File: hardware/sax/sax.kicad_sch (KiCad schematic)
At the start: 36 parts, among them J101 Cortex, J102 DX07S016JA3, SW101 SKSG, SW102 SKSG, U101 TPS78433QWDRBRQ1, U102 ATSAMD51J, Y101 32k768

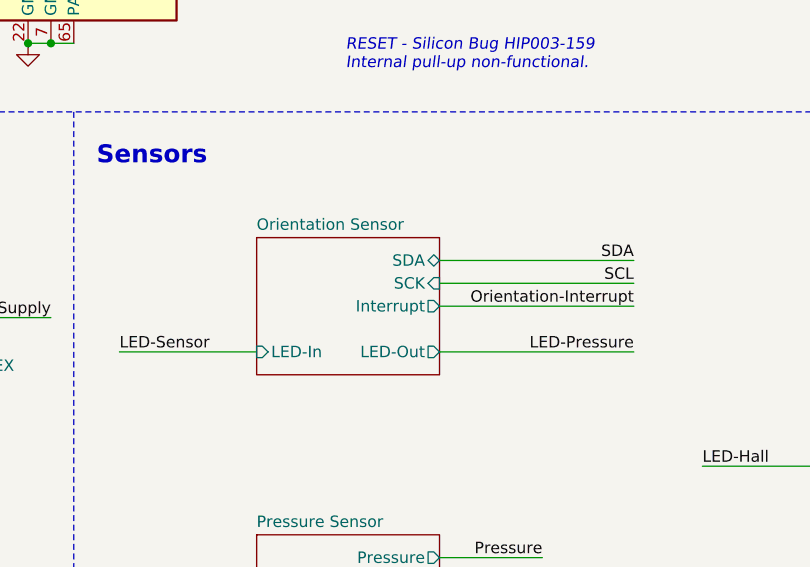
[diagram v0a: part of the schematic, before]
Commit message: KiCad 10
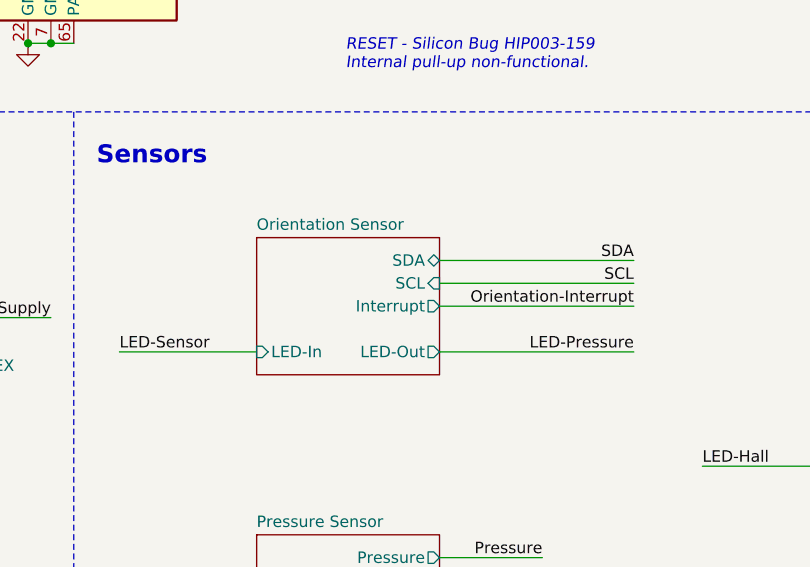
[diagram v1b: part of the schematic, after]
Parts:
- INFO101: value ~ -> (none)
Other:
- sheet Orientation Sensor ports: added SCL; removed SCK

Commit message: Refresh
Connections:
- net VDDCORE renamed +VDDCORE
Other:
- moved on the sheet: TVS101

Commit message: Replace step-down
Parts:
- C107, C110: Rating (none) -> 50V
- SW101, SW102: Rating (none) -> 1.6N
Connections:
- net USB+: now also ESD101.3 (D1)
- net USB-: now also ESD101.2 (D2)
- no-connect marks 33 -> 31
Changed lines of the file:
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@@
 	(title_block
 		(title "V2 sax")
-		(date "2026-03-21")
-		(rev "2026-02-10")
+		(date "2026-03-31")
+		(rev "2026-03-31")
 		(company "Versio Duo")
 		(comment 1 "Saxophone Controller")
@@
 		(color 0 0 0 0)
 	)
+	(junction
+		(at 247.65 91.44)
+		(diameter 0)
+		(color 0 0 0 0)
+	)
+	(junction
+		(at 247.65 83.82)
+		(diameter 0)
+		(color 0 0 0 0)
+	)
 	(no_connect
 		(at 86.36 59.69)
@@
 	)
 	(no_connect
-		(at 247.65 86.36)
-	)
-	(no_connect
 		(at 53.34 67.31)
 	)
@@
 	)
 	(no_connect
-		(at 247.65 93.98)
-	)
-	(no_connect
 		(at 53.34 44.45)
 	)
@@
 	(wire
 		(pts
+			(xy 247.65 91.44) (xy 247.65 93.98)
+		)
+		(stroke
+			(width 0)
+			(type default)
+		)
+	)
+	(wire
+		(pts
 			(xy 31.75 105.41) (xy 53.34 105.41)
 		)
@@
 	(wire
 		(pts
+			(xy 247.65 83.82) (xy 247.65 86.36)
+		)
+		(stroke
+			(width 0)
+			(type default)
+		)
+	)
+	(wire
+		(pts
 			(xy 31.75 80.01) (xy 53.34 80.01)
 		)
@@
 			)
 		)
+		(property "Rating" "1.6N"
+			(at 247.65 48.26 0)
+			(hide yes)
+			(show_name no)
+			(do_not_autoplace no)
+			(effects
+				(font
+					(size 1.27 1.27)
+				)
+			)
+		)
 		(pin "1"
 		)
@@
 			)
 		)
+		(property "Rating" "50V"
+			(at -1.27 43.18 0)
+			(hide yes)
+			(show_name no)
+			(do_not_autoplace no)
+			(effects
+				(font
+					(size 1.27 1.27)
+				)
+			)
+		)
 		(pin "1"
 		)
@@
 		(in_bom no)
 		(on_board no)
-		(in_pos_files yes)
+		(in_pos_files no)
 		(dnp no)
 		(property "Reference" "#PWR138"
@@
 		(in_bom no)
 		(on_board no)
-		(in_pos_files yes)
+		(in_pos_files no)
 		(dnp no)
 		(property "Reference" "#PWR118"
@@
 		(in_bom no)
 		(on_board no)
-		(in_pos_files yes)
+		(in_pos_files no)
 		(dnp no)
 		(fields_autoplaced yes)
@@
 		(in_bom no)
 		(on_board no)
-		(in_pos_files yes)
+		(in_pos_files no)
 		(dnp no)
 		(fields_autoplaced yes)
@@
 		(in_bom no)
 		(on_board no)
-		(in_pos_files yes)
+		(in_pos_files no)
 		(dnp no)
 		(property "Reference" "#PWR140"
@@
 		(in_bom no)
 		(on_board no)
-		(in_pos_files yes)
+		(in_pos_files no)
 		(dnp no)
 		(property "Reference" "#PWR126"
@@
 			)
 		)
+		(property "Rating" "50V"
+			(at -1.27 38.1 0)
+			(hide yes)
+			(show_name no)
+			(do_not_autoplace no)
+			(effects
+				(font
+					(size 1.27 1.27)
+				)
+			)
+		)
 		(pin "1"
 		)
@@
 		(in_bom no)
 		(on_board no)
-		(in_pos_files yes)
+		(in_pos_files no)
 		(dnp no)
 		(property "Reference" "#PWR137"
@@
 			)
 		)
+		(property "Rating" "1.6N"
+			(at 133.35 96.52 0)
+			(hide yes)
+			(show_name no)
+			(do_not_autoplace no)
+			(effects
+				(font
+					(size 1.27 1.27)
+				)
+			)
+		)
 		(pin "1"
 		)
@@
 		(in_bom no)
 		(on_board no)
-		(in_pos_files yes)
+		(in_pos_files no)
 		(dnp no)
 		(fields_autoplaced yes)
@@
 		(in_bom no)
 		(on_board no)
-		(in_pos_files yes)
+		(in_pos_files no)
 		(dnp no)
 		(property "Reference" "#PWR131"

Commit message: Limit up note length to 3 seconds
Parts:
- C101, C102, C103, C104, C105, C106, C107, C108, C109, C110, C111: Id (none) -> Capacitor:${SYMBOL_NAME}
- D101, D102: Id (none) -> LED:${SYMBOL_NAME}
- D103, D104, D105, TVS101: Id (none) -> Diode:${SYMBOL_NAME}
- ESD101: Id (none) -> ESD:${SYMBOL_NAME}
- J102: Id (none) -> USB:${SYMBOL_NAME}
- R101, R102, R103, R104: Id (none) -> Resistor:${SYMBOL_NAME}
- SW101, SW102: Id (none) -> Button:${SYMBOL_NAME}
- U101: Id (none) -> LDO:${SYMBOL_NAME}
- U102: Id (none) -> MCU:${SYMBOL_NAME}
- Y101: Id (none) -> Crystal:${SYMBOL_NAME}

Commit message: Update
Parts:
- D101: Rating (none) -> 15mA
- D102: Rating (none) -> 605nm
- J102: Rating (none) -> USB2.0
- U101: Rating (none) -> 300mA
- Y101: Rating (none) -> 10ppm
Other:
- moved on the sheet: C111, D105, TVS101

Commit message: Update
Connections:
- net +VDDCORE renamed +VCORE
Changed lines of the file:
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@@
 		)
 	)
-	(label "+VDDCORE"
+	(label "+VCORE"
 		(at 58.42 24.13 0)
 		(effects
